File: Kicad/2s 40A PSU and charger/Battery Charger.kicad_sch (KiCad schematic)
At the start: 43 parts, among them Q1 PJA3430, Q2 PJA3430, Q3 Vishay sir404dp, Q4 PJA3430, Q5 PJA3430, U3 BQ24780SRUYR

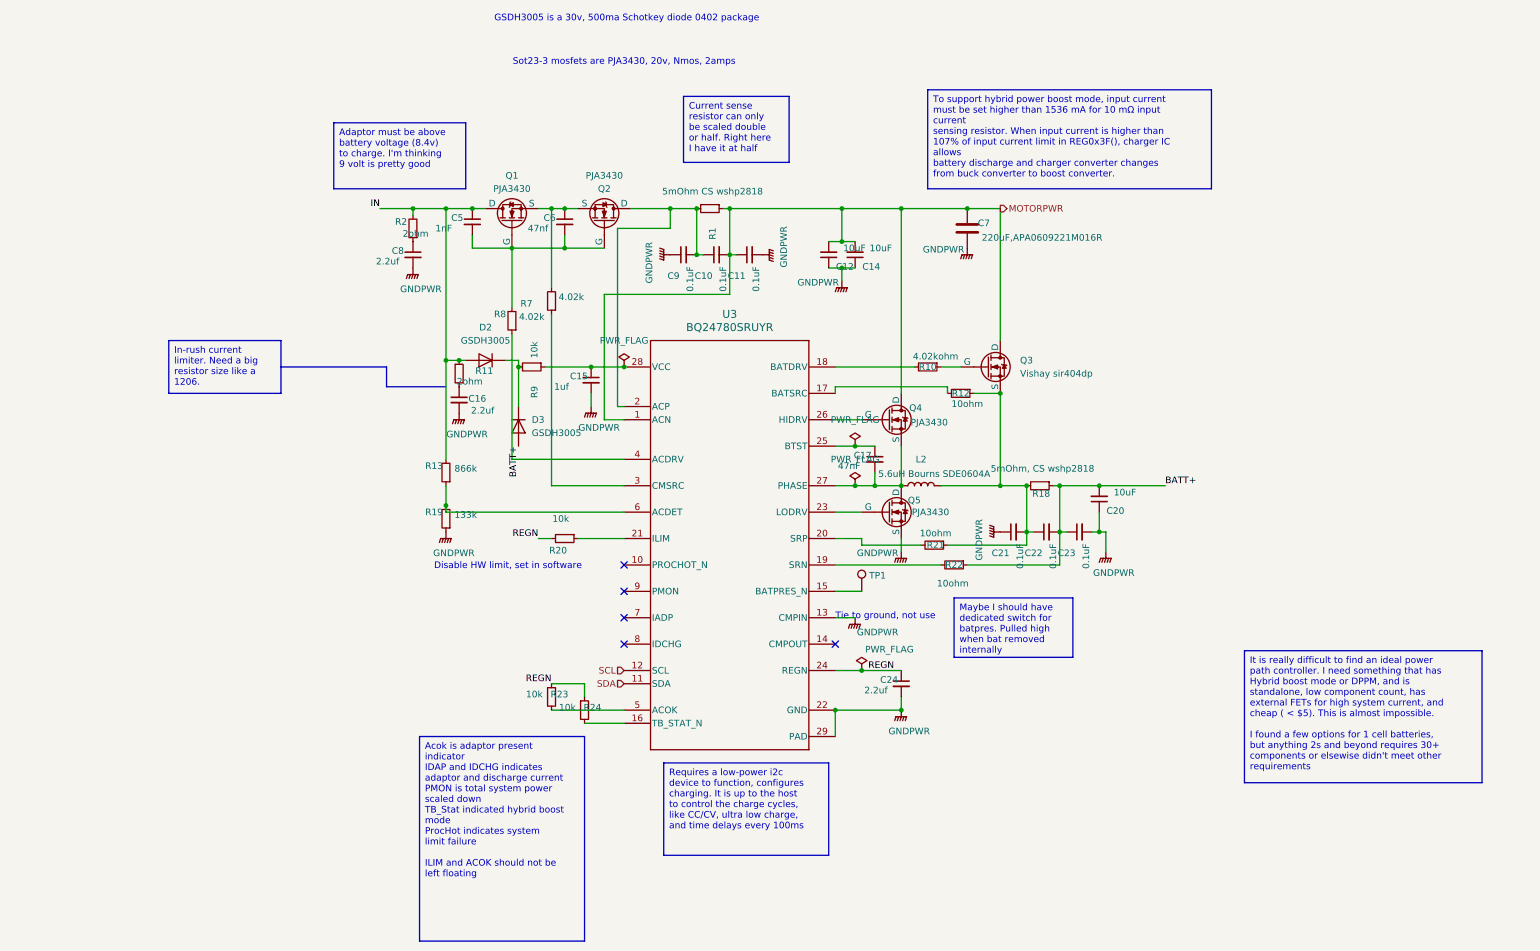
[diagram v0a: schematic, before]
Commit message: Reworked PSU to use CH32X035 and USB-PD
This will save a few bucks and will actually be a cooler solution than just a DC jack connected to some pads
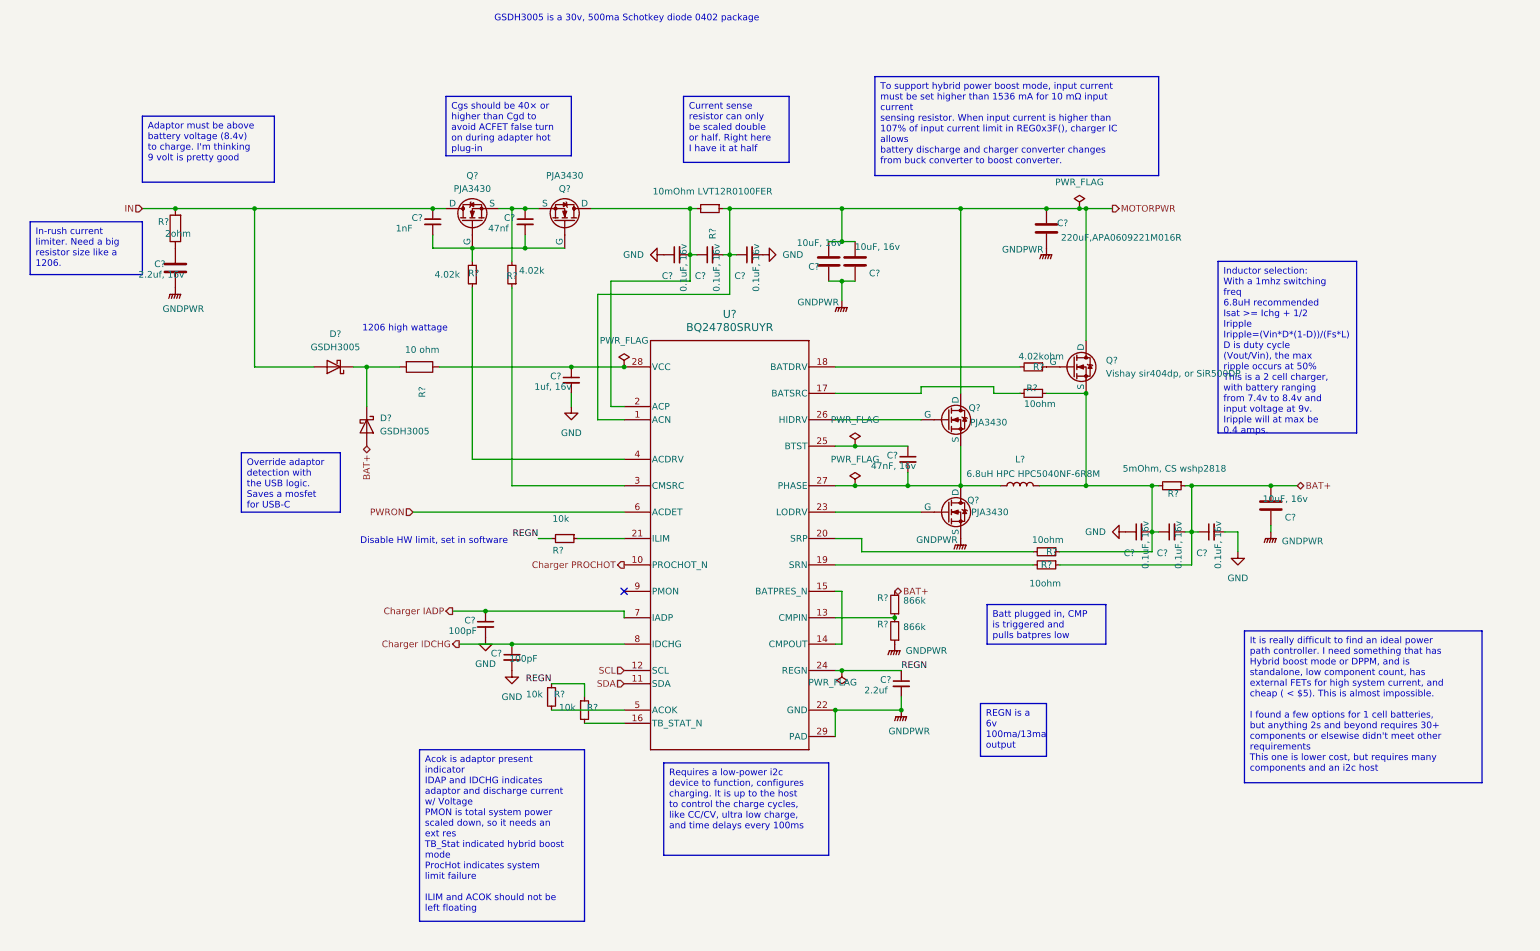
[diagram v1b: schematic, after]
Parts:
- removed C16: 2.2uf, Capacitor_SMD:C_0603_1608Metric, symbol Device:C_Small
- removed R11: 2ohm, Resistor_SMD:R_0603_1608Metric, symbol Device:R_Small
- removed R13: 866k, Resistor_SMD:R_0603_1608Metric, symbol Device:R_Small
- removed R19: 133k, Resistor_SMD:R_0603_1608Metric, symbol Device:R_Small
- removed TP1: ~, TestPoint:TestPoint_Pad_D1.0mm, symbol Connector:TestPoint
- added C? (x2): 100pF, Capacitor_SMD:C_0402_1005Metric, symbol Device:C_Small
- added R? (x2): 866k, Resistor_SMD:R_0402_1005Metric, symbol Device:R_Small
- C?: renamed from C8; value 2.2uf -> 2.2uf, 16v; footprint Capacitor_SMD:C_0603_1608Metric -> Capacitor_SMD:C_1206_3216Metric; symbol Device:C_Small -> Device:C
- C?: renamed from C23; value 0.1uF -> 0.1uF, 16v; footprint Capacitor_SMD:C_0603_1608Metric -> Capacitor_SMD:C_0402_1005Metric
- C?: renamed from C22; value 0.1uF -> 0.1uF, 16v; footprint Capacitor_SMD:C_0603_1608Metric -> Capacitor_SMD:C_0402_1005Metric
- C?: renamed from C17; value 47nF -> 47nF, 16v
- C?: renamed from C10; value 0.1uF -> 0.1uF, 16v; footprint Capacitor_SMD:C_0603_1608Metric -> Capacitor_SMD:C_0402_1005Metric
- C?: renamed from C11; value 0.1uF -> 0.1uF, 16v; footprint Capacitor_SMD:C_0603_1608Metric -> Capacitor_SMD:C_0402_1005Metric
- C?: renamed from C9; value 0.1uF -> 0.1uF, 16v; footprint Capacitor_SMD:C_0603_1608Metric -> Capacitor_SMD:C_0402_1005Metric
- C?: renamed from C14; value 10uF -> 10uF, 16v; footprint Capacitor_SMD:C_0603_1608Metric -> Capacitor_SMD:C_0805_2012Metric; symbol Device:C_Small -> Device:C
- C?: renamed from C5; footprint Capacitor_SMD:C_0603_1608Metric -> Capacitor_SMD:C_0402_1005Metric
- C?: renamed from C20; value 10uF -> 10uF, 16v; footprint Capacitor_SMD:C_0603_1608Metric -> Capacitor_SMD:C_0805_2012Metric; symbol Device:C_Small -> Device:C
- C?: renamed from C21; value 0.1uF -> 0.1uF, 16v; footprint Capacitor_SMD:C_0603_1608Metric -> Capacitor_SMD:C_0402_1005Metric
- C?: renamed from C12; value 10uF -> 10uF, 16v; footprint Capacitor_SMD:C_0603_1608Metric -> Capacitor_SMD:C_0805_2012Metric; symbol Device:C_Small -> Device:C
- C?: renamed from C15; value 1uf -> 1uf, 16v; footprint Capacitor_SMD:C_0603_1608Metric -> Capacitor_SMD:C_0402_1005Metric
- D?: renamed from D3; symbol Device:D -> Device:D_Schottky
- D?: renamed from D2; symbol Device:D -> Device:D_Schottky
- L?: renamed from L2; value 5.6uH Bourns SDE0604A -> 6.8uH HPC HPC5040NF-6R8M
- Q?: renamed from Q3; value Vishay sir404dp -> Vishay sir404dp, or SiR500DP
- R?: renamed from R22; footprint Resistor_SMD:R_0603_1608Metric -> Resistor_SMD:R_0402_1005Metric
- R?: renamed from R2; footprint Resistor_SMD:R_0603_1608Metric -> Resistor_SMD:R_1206_3216Metric; symbol Device:R_Small -> Device:R
- R?: renamed from R9; value 10k -> 10 ohm; footprint Resistor_SMD:R_0603_1608Metric -> Resistor_SMD:R_0805_2012Metric; symbol Device:R_Small -> Device:R
- R?: renamed from R21; footprint Resistor_SMD:R_0603_1608Metric -> Resistor_SMD:R_0402_1005Metric
- R?: renamed from R10; footprint Resistor_SMD:R_0603_1608Metric -> Resistor_SMD:R_0402_1005Metric
- R?: renamed from R1; value 5mOhm CS wshp2818 -> 10mOhm LVT12R0100FER; footprint Resistor_SMD:R_2816_7142Metric -> Resistor_SMD:R_1206_3216Metric
- R?: renamed from R7; footprint Resistor_SMD:R_0603_1608Metric -> Resistor_SMD:R_0402_1005Metric
- R?: renamed from R8; footprint Resistor_SMD:R_0603_1608Metric -> Resistor_SMD:R_0402_1005Metric
- R?: renamed from R12; footprint Resistor_SMD:R_0603_1608Metric -> Resistor_SMD:R_0402_1005Metric
- R?: renamed from R20; footprint Resistor_SMD:R_0603_1608Metric -> Resistor_SMD:R_0402_1005Metric
- R?: renamed from R24; footprint Resistor_SMD:R_0603_1608Metric -> Resistor_SMD:R_0402_1005Metric
- R?: renamed from R23; footprint Resistor_SMD:R_0603_1608Metric -> Resistor_SMD:R_0402_1005Metric
- renumbered C6 to C?, C7 to C?, C24 to C?, Q5 to Q?, Q4 to Q?, Q2 to Q?, Q1 to Q?, R18 to R?, U3 to U?
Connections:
- net GNDPWR: now also R?.1; no longer C?.1, C?.1, C?.2, C?.2, C?.2, U?.13 (CMPIN)
- net PWRON: now reaches U?.6 (ACDET)
- net at U?.15 (BATPRES_N): now also U?.14 (CMPOUT)
- net Charger PROCHOT: now reaches U?.10 (PROCHOT_N)
- net Charger IADP: now reaches U?.7 (IADP)
- net Charger IADP: now also C?.1
- net Charger IDCHG: now reaches U?.8 (IDCHG)
- net Charger IDCHG: now also C?.1
- net BATT+ renamed BAT+
- net BAT+: now also R?.2
- new net: R?.1, R?.2, U?.13 (CMPIN)
- new net GND: C?.1, C?.1, C?.2, C?.2, C?.2, C?.2, C?.2
- no-connect marks 5 -> 1
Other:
- note added: "1206 high wattage"
- note removed: "Sot23-3 mosfets are PJA3430, 20v, Nmos, 2amps"
- note removed: "Tie to ground, not use"
- moved on the sheet: C?, D?, L?, Q?, R?

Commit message: Improved schematic formatting and visuals
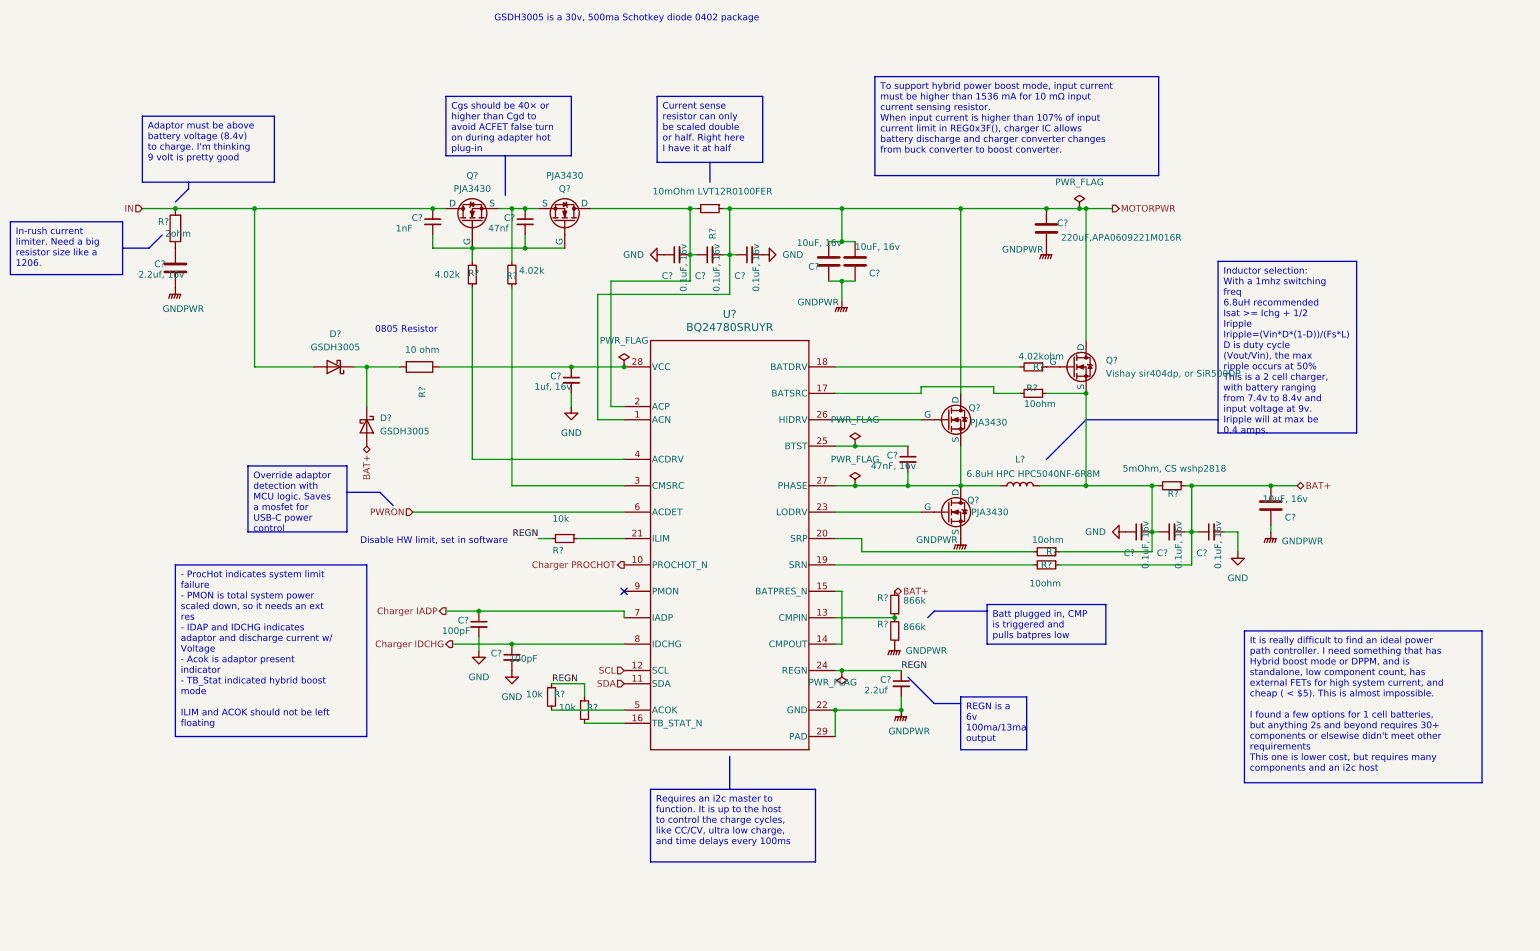
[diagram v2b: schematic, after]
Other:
- note added: "0805 Resistor"
- note removed: "1206 high wattage"
- moved on the sheet: C?
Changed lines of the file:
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@@
 	)
 	(junction
-		(at 85.09 132.08)
-		(diameter 0)
-		(color 0 0 0 0)
-	)
-	(junction
 		(at 132.08 54.61)
 		(diameter 0)
@@
 	)
 	(junction
+		(at 83.82 132.08)
+		(diameter 0)
+		(color 0 0 0 0)
+	)
+	(junction
 		(at 213.36 116.84)
 		(diameter 0)
@@
 		(at 111.76 128.27)
 	)
+	(polyline
+		(pts
+			(xy 58.42 109.22) (xy 64.77 109.22)
+		)
+		(stroke
+			(width 0)
+			(type default)
+		)
+	)
+	(polyline
+		(pts
+			(xy 27.94 49.53) (xy 27.94 50.8)
+		)
+		(stroke
+			(width 0)
+			(type default)
+		)
+	)
 	(wire
 		(pts
@@
 		)
 	)
+	(polyline
+		(pts
+			(xy 132.08 160.02) (xy 132.08 166.37)
+		)
+		(stroke
+			(width 0)
+			(type default)
+		)
+	)
 	(wire
 		(pts
@@
 		)
 	)
+	(polyline
+		(pts
+			(xy 64.77 109.22) (xy 67.31 111.76)
+		)
+		(stroke
+			(width 0)
+			(type default)
+		)
+	)
 	(wire
 		(pts
@@
 		)
 	)
+	(polyline
+		(pts
+			(xy 166.37 144.78) (xy 171.45 149.86)
+		)
+		(stroke
+			(width 0)
+			(type default)
+		)
+	)
 	(wire
 		(pts
@@
 		)
 	)
+	(polyline
+		(pts
+			(xy 193.04 102.87) (xy 200.66 95.25)
+		)
+		(stroke
+			(width 0)
+			(type default)
+		)
+	)
 	(wire
 		(pts
@@
 		)
 	)
+	(polyline
+		(pts
+			(xy 181.61 132.08) (xy 171.45 132.08)
+		)
+		(stroke
+			(width 0)
+			(type default)
+		)
+	)
+	(polyline
+		(pts
+			(xy 176.53 149.86) (xy 171.45 149.86)
+		)
+		(stroke
+			(width 0)
+			(type default)
+		)
+	)
 	(wire
 		(pts
@@
 	(wire
 		(pts
+			(xy 83.82 132.08) (xy 111.76 132.08)
+		)
+		(stroke
+			(width 0)
+			(type default)
+		)
+	)
+	(wire
+		(pts
 			(xy 152.4 113.03) (xy 168.91 113.03)
 		)
@@
 	(wire
 		(pts
+			(xy 83.82 137.16) (xy 83.82 139.7)
+		)
+		(stroke
+			(width 0)
+			(type default)
+		)
+	)
+	(wire
+		(pts
 			(xy 153.67 68.58) (xy 153.67 72.39)
 		)
@@
 	(wire
 		(pts
-			(xy 78.74 132.08) (xy 85.09 132.08)
+			(xy 77.47 132.08) (xy 83.82 132.08)
 		)
 		(stroke
@@
 		)
 	)
-	(wire
+	(polyline
 		(pts
-			(xy 152.4 133.35) (xy 163.83 133.35)
+			(xy 170.18 133.35) (xy 171.45 132.08)
 		)
 		(stroke
@@
 	(wire
 		(pts
-			(xy 124.46 63.5) (xy 124.46 68.58)
+			(xy 152.4 133.35) (xy 163.83 133.35)
 		)
 		(stroke
@@
 	(wire
 		(pts
-			(xy 104.14 146.05) (xy 97.79 146.05)
+			(xy 124.46 63.5) (xy 124.46 68.58)
 		)
 		(stroke
@@
 	(wire
 		(pts
-			(xy 85.09 132.08) (xy 111.76 132.08)
+			(xy 152.4 118.11) (xy 157.48 118.11)
 		)
 		(stroke
@@
 		)
 	)
-	(wire
+	(polyline
 		(pts
-			(xy 152.4 118.11) (xy 157.48 118.11)
+			(xy 226.06 95.25) (xy 200.66 95.25)
 		)
 		(stroke
@@
 		)
 	)
+	(polyline
+		(pts
+			(xy 20.32 62.23) (xy 22.86 59.69)
+		)
+		(stroke
+			(width 0)
+			(type default)
+		)
+	)
 	(wire
 		(pts
@@
 		)
 	)
+	(polyline
+		(pts
+			(xy 88.9 44.45) (xy 88.9 52.07)
+		)
+		(stroke
+			(width 0)
+			(type default)
+		)
+	)
 	(wire
 		(pts
@@
 	(wire
 		(pts
+			(xy 97.79 146.05) (xy 104.14 146.05)
+		)
+		(stroke
+			(width 0)
+			(type default)
+		)
+	)
+	(wire
+		(pts
 			(xy 236.22 107.95) (xy 241.3 107.95)
 		)
@@
 		)
 	)
+	(polyline
+		(pts
+			(xy 128.27 45.72) (xy 128.27 49.53)
+		)
+		(stroke
+			(width 0)
+			(type default)
+		)
+	)
 	(wire
 		(pts
@@
 	(wire
 		(pts
-			(xy 80.01 138.43) (xy 90.17 138.43)
+			(xy 78.74 138.43) (xy 90.17 138.43)
 		)
 		(stroke
@@
 		)
 	)
+	(polyline
+		(pts
+			(xy 25.4 53.34) (xy 27.94 50.8)
+		)
+		(stroke
+			(width 0)
+			(type default)
+		)
+	)
 	(wire
 		(pts
@@
 		)
 	)
+	(polyline
+		(pts
+			(xy 15.24 62.23) (xy 20.32 62.23)
+		)
+		(stroke
+			(width 0)
+			(type default)
+		)
+	)
 	(wire
 		(pts
@@
 		)
 	)
-	(text_box "To support hybrid power boost mode, input current must be set higher than 1536 mA for 10 mΩ input current\nsensing resistor. When input current is higher than 107% of input current limit in REG0x3F(), charger IC allows\nbattery discharge and charger converter changes from buck converter to boost converter."
+	(text_box "To support hybrid power boost mode, input current must be higher than 1536 mA for 10 mΩ input current sensing resistor.\nWhen input current is higher than 107% of input current limit in REG0x3F(), charger IC allows\nbattery discharge and charger converter changes from buck converter to boost converter."
 		(exclude_from_sim no)
 		(at 160.02 29.21 0)
@@
 		)
 	)
-	(text_box "Requires a low-power i2c device to function, configures charging. It is up to the host to control the charge cycles, like CC/CV, ultra low charge, and time delays every 100ms"
+	(text_box "Requires an i2c master to function. It is up to the host to control the charge cycles, like CC/CV, ultra low charge, and time delays every 100ms"
 		(exclude_from_sim no)
-		(at 119.38 161.29 0)
-		(size 31.75 17.78)
+		(at 116.84 166.37 0)
+		(size 31.75 13.97)
 		(stroke
 			(width 0)
@@
 	(text_box "Current sense resistor can only be scaled double or half. Right here I have it at half"
 		(exclude_from_sim no)
-		(at 123.19 33.02 0)
+		(at 118.11 33.02 0)
 		(size 20.32 12.7)
 		(stroke
@@
 	(text_box "In-rush current limiter. Need a big resistor size like a 1206."
 		(exclude_from_sim no)
-		(at -2.54 57.15 0)
+		(at -6.35 57.15 0)
 		(size 21.59 10.16)
 		(stroke
@@
 		)
 	)
-	(text_box "Override adaptor detection with the USB logic. Saves a mosfet for USB-C"
+	(text_box "Override adaptor detection with MCU logic. Saves a mosfet for USB-C power control"
 		(exclude_from_sim no)
-		(at 38.1 101.6 0)
-		(size 19.05 11.43)
+		(at 39.37 104.14 0)
+		(size 19.05 12.7)
 		(stroke
 			(width 0)
@@
 	(text_box "REGN is a 6v 100ma/13ma output"
 		(exclude_from_sim no)
-		(at 180.34 149.86 0)
+		(at 176.53 148.59 0)
 		(size 12.7 10.16)
 		(stroke
@@
 		)
 	)
-	(text_box "Acok is adaptor present indicator\nIDAP and IDCHG indicates adaptor and discharge current w/ Voltage\nPMON is total system power scaled down, so it needs an ext res\nTB_Stat indicated hybrid boost mode\nProcHot indicates system limit failure\n\nILIM and ACOK should not be left floating "
+	(text_box "- ProcHot indicates system limit failure\n- PMON is total system power scaled down, so it needs an ext res\n- IDAP and IDCHG indicates adaptor and discharge current w/ Voltage\n- Acok is adaptor present indicator\n- TB_Stat indicated hybrid boost mode\n\nILIM and ACOK should not be left floating "
 		(exclude_from_sim no)
-		(at 72.39 158.75 0)
-		(size 31.75 33.02)
+		(at 25.4 123.19 0)
+		(size 36.83 33.02)
 		(stroke
 			(width 0)
@@
 		)
 	)
-	(text "1206 high wattage"
+	(text "0805 Resistor"
 		(exclude_from_sim no)
-		(at 69.596 77.724 0)
+		(at 69.85 77.978 0)
 		(effects
 			(font
@@
 	)
 	(label "REGN"
-		(at 97.79 146.05 180)
+		(at 102.87 146.05 180)
 		(fields_autoplaced yes)
 		(effects
@@
 	(hierarchical_label "Charger IADP"
 		(shape output)
-		(at 78.74 132.08 180)
+		(at 77.47 132.08 180)
 		(fields_autoplaced yes)
 		(effects
@@
 	(hierarchical_label "Charger IDCHG"
 		(shape output)
-		(at 80.01 138.43 180)
+		(at 78.74 138.43 180)
 		(fields_autoplaced yes)
 		(effects
@@
 	(symbol
 		(lib_id "power:GND")
-		(at 85.09 137.16 0)
+		(at 83.82 139.7 0)
 		(unit 1)
 		(exclude_from_sim no)
@@
 		(fields_autoplaced yes)
 		(property "Reference" "#PWR?"
-			(at 85.09 143.51 0)
+			(at 83.82 146.05 0)
 			(effects
 				(font
@@
 		)
 		(property "Value" "GND"
-			(at 85.09 142.24 0)
+			(at 83.82 144.78 0)
 			(effects
 				(font
@@
 		)
 		(property "Footprint" ""
-			(at 85.09 137.16 0)
+			(at 83.82 139.7 0)
 			(effects
 				(font
@@
 		)
 		(property "Datasheet" ""
-			(at 85.09 137.16 0)
+			(at 83.82 139.7 0)
 			(effects
 				(font
@@
 		)
 		(property "Description" "Power symbol creates a global label with name \"GND\" , ground"
-			(at 85.09 137.16 0)
+			(at 83.82 139.7 0)
 			(effects
 				(font
@@
 	(symbol
 		(lib_id "Device:C_Small")
-		(at 85.09 134.62 0)
+		(at 83.82 134.62 0)
 		(unit 1)
 		(exclude_from_sim no)
@@
 		(dnp no)
 		(property "Reference" "C?"
-			(at 81.026 133.858 0)
+			(at 79.756 133.858 0)
 			(effects
 				(font
@@
 		)
 		(property "Value" "100pF"
-			(at 77.978 135.89 0)
+			(at 76.708 135.89 0)
 			(effects
 				(font
@@
 		)
 		(property "Footprint" "Capacitor_SMD:C_0402_1005Metric"
-			(at 85.09 134.62 0)
+			(at 83.82 134.62 0)
 			(effects
 				(font
@@
 		)
 		(property "Datasheet" "~"
-			(at 85.09 134.62 0)
+			(at 83.82 134.62 0)
 			(effects
 				(font
@@
 		)
 		(property "Description" "Unpolarized capacitor, small symbol"
-			(at 85.09 134.62 0)
+			(at 83.82 134.62 0)
 			(effects
 				(font
